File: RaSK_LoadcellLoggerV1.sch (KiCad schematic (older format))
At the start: 31 parts, among them P1 STLINK_SWD, U1 STM32F303RE, U2 TWE-Lite_DIP

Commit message: complete making schematic
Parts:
- removed C2: 0.47u, symbol C_Small
- removed VR1: NJM12888, TO_SOT_Packages_SMD:SOT-23-5, symbol NJM12888
- added C2, C4: 33u, symbol CP_Small
- added C3: 0.1u, symbol C_Small
- added J1: LoadCell, symbol Conn_01x05_Female
- added U3: Sparkfun_HX711_LoadCellAmp, KUT_Sensor:Sparkfun_HX711_LoadCellAmp_Module, symbol Sparkfun_HX711_LoadCellAmp
- added VR1, VR2: TA48Mxx, symbol TA48Mxx
- gave numbers to parts that had none: 8
- renumbered C2 to C5, C3 to C6, C4 to C7, C5 to C8, C6 to C9
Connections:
- net labels added: +5V, LCAmp_DAT, LCAmp_SCK
- wire segments 79 -> 94
- no-connect marks 39 -> 38
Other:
- moved on the sheet: P1

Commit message: connect stm32 pins to other components except for loadcell-amp (Sorry, I forgot this step...) add STLink UART debug connector add two buttons for TWE-Lite programming
p.s.
I didn't connect communication pins of loadcell-amp.
These pins can connect any stm32 digital pins.
Please connect these pins as you want.
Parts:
- removed J1: LoadCell, symbol Conn_01x05_Female
- added J1: STLINK_UART, symbol Conn_01x03_Male
- added J2: Conn_01x05_Male, symbol Conn_01x05_Male
- added SW1: TWE_RESET, symbol SW_Push
- added SW2: TWE_PRG, symbol SW_Push
- renumbered J6 to J3, J2 to J4, J4 to J5, J3 to J6, J5 to J7
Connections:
- net labels added: Debug_mIN, Debug_mOUT, TWE_mIN, TWE_mOUT
- net labels removed: TWE_MIN, TWE_MOUT, TWE_PRG, TWE_RESET
- wire segments 94 -> 103
- no-connect marks 38 -> 72

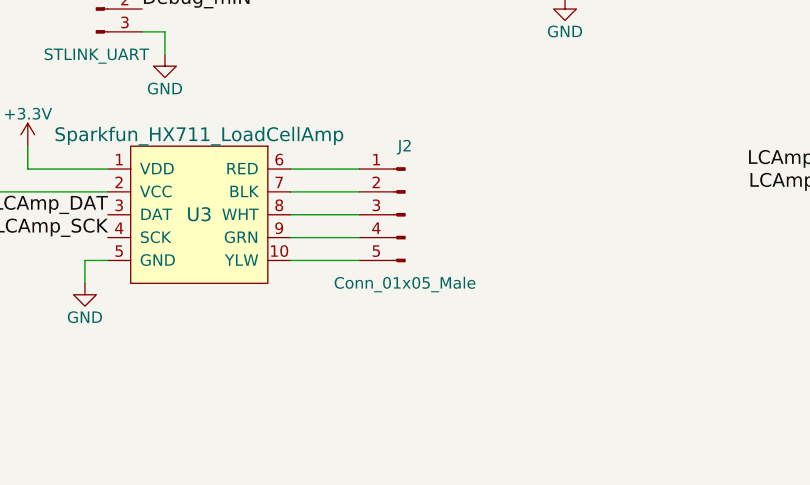
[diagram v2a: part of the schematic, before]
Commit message: fix connector J2 name
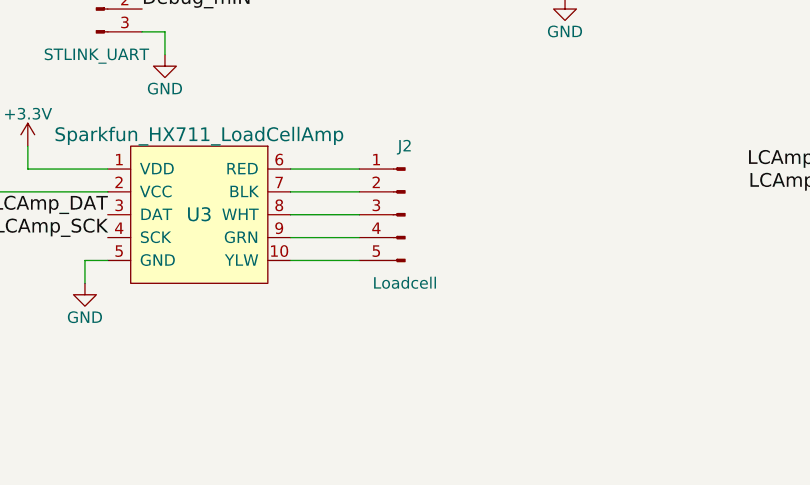
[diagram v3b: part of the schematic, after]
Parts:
- J2: value Conn_01x05_Male -> Loadcell
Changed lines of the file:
@@
 P 3050 6300
 F 0 "J2" H 3050 6600 50  0000 C CNN
-F 1 "Conn_01x05_Male" H 3050 6000 50  0000 C CNN
+F 1 "Loadcell" H 3050 6000 50  0000 C CNN
 F 2 "" H 3050 6300 50  0001 C CNN
 F 3 "" H 3050 6300 50  0001 C CNN

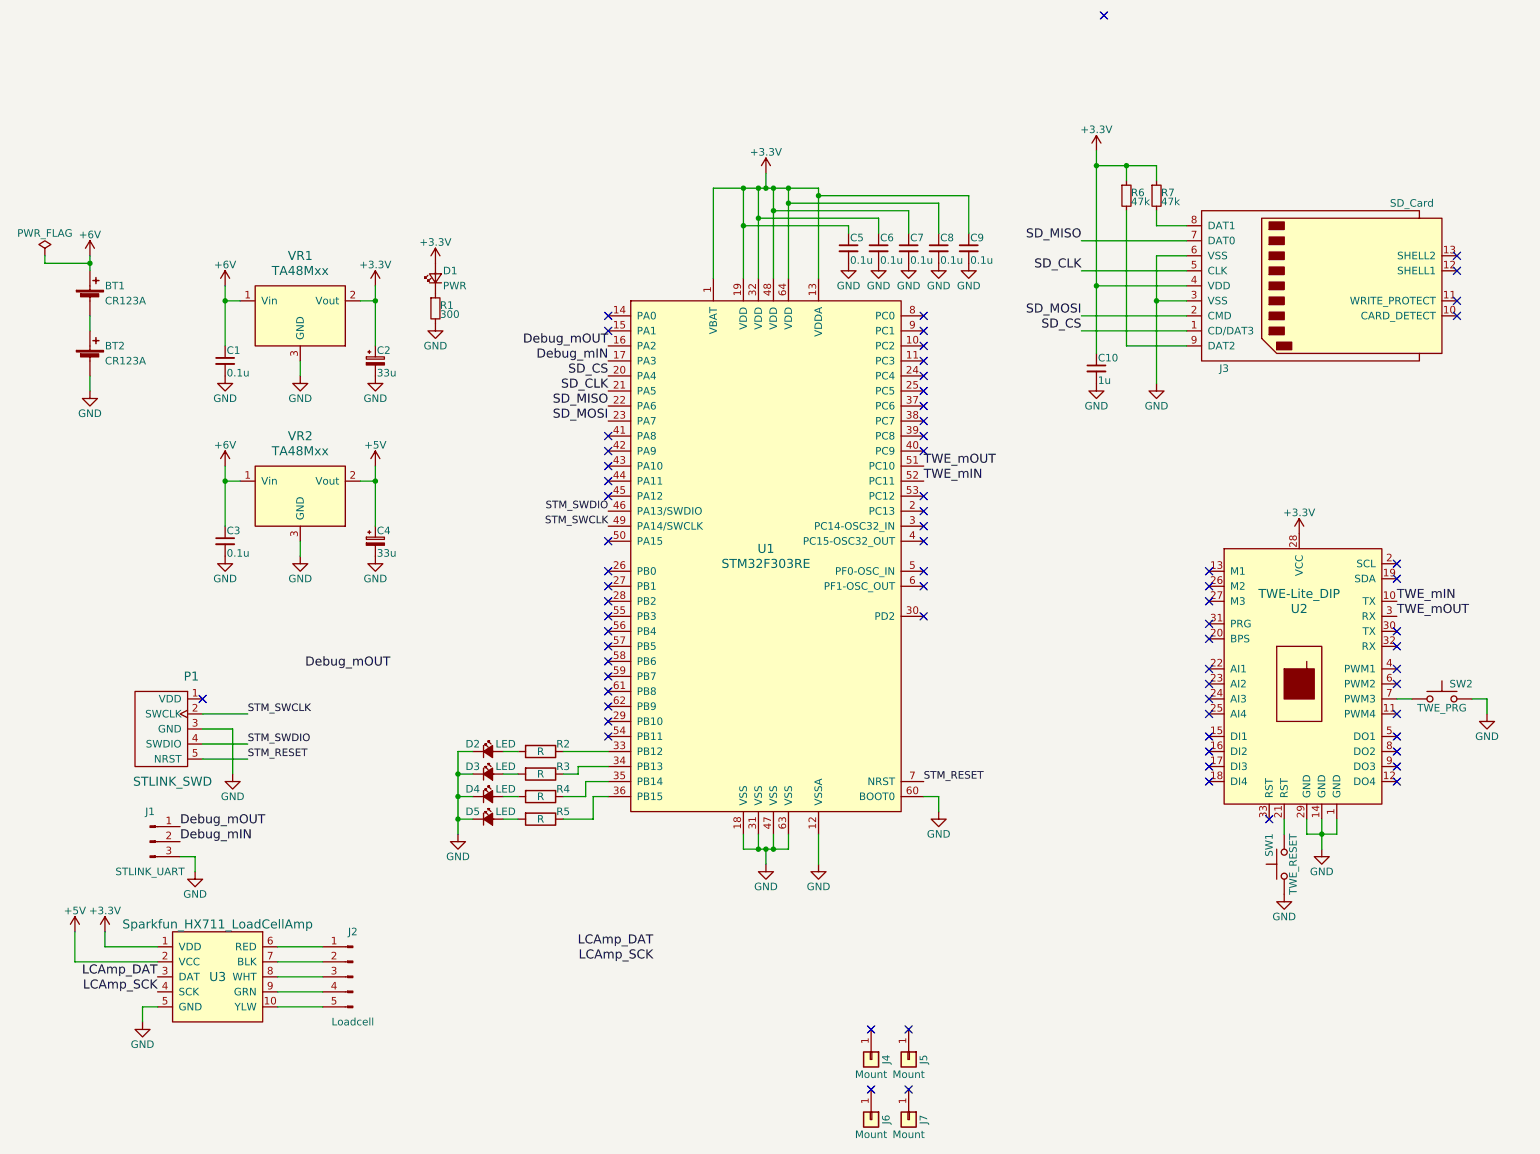
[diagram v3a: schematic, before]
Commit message: add power switch ,pass capacitor and assign footprint
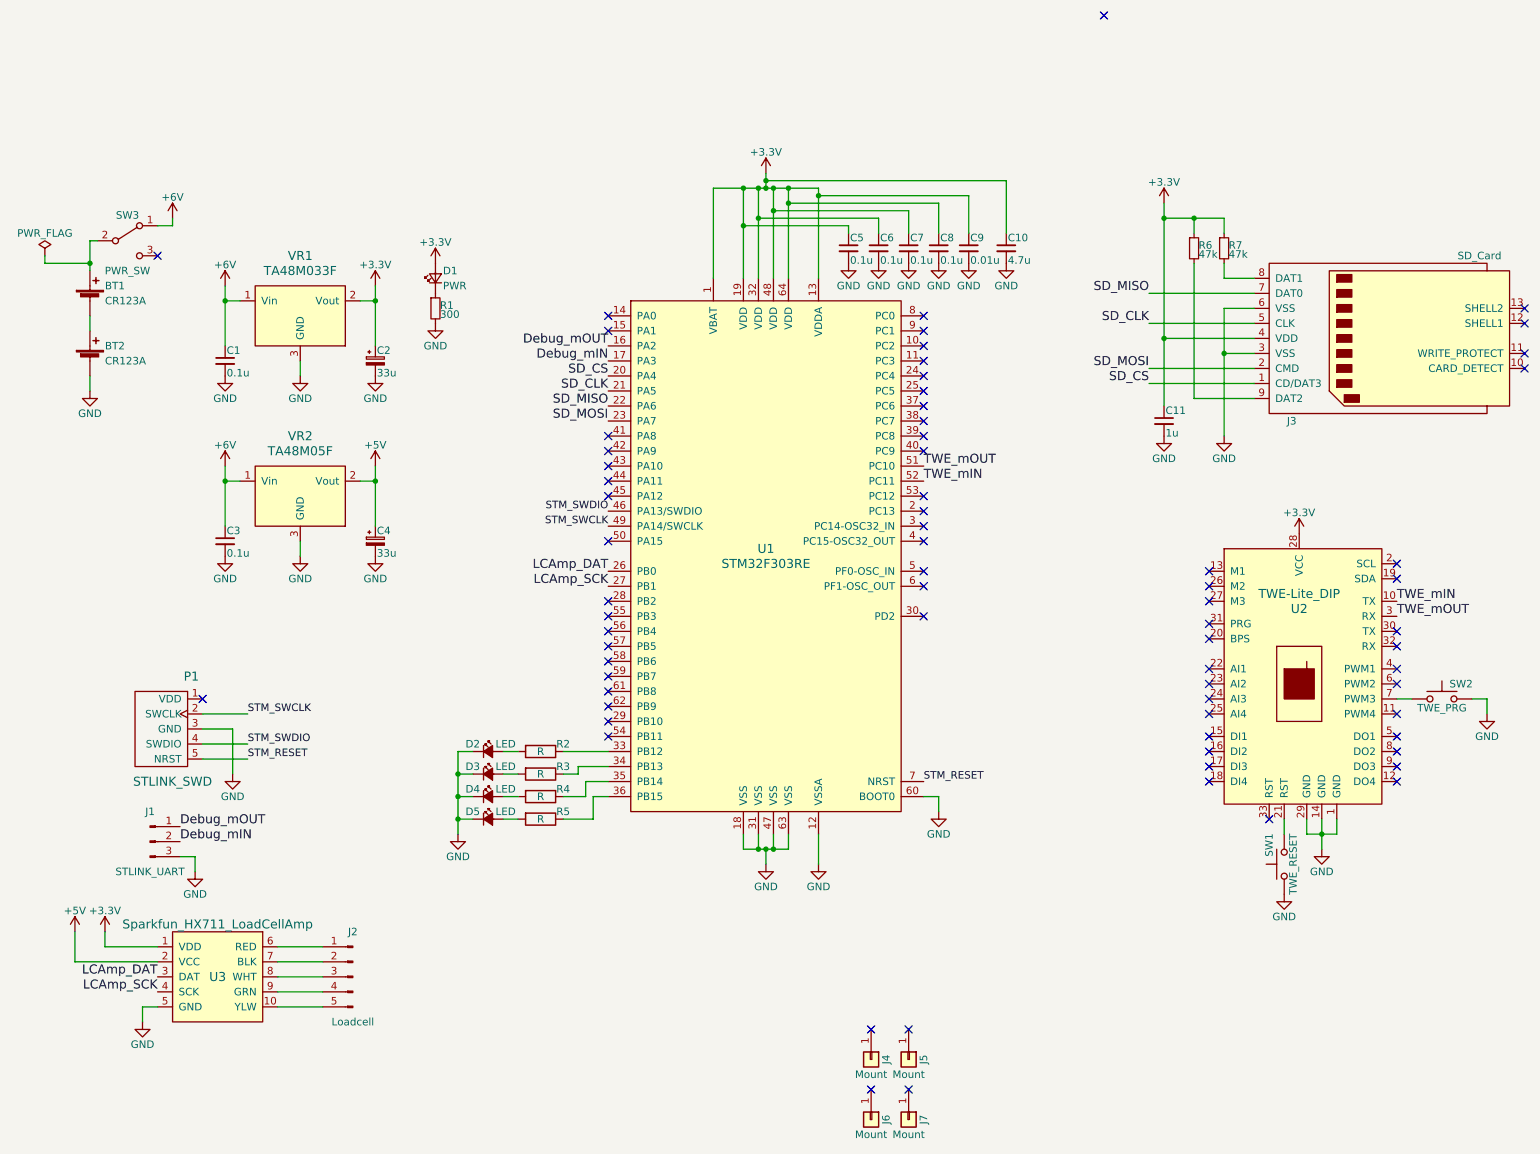
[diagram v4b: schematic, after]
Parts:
- added C10: 4.7u, Capacitors_SMD:C_1206, symbol C_Small
- added SW3: PWR_SW, KUT_Switch:ToggleSeitch_Q22, symbol SW_SPDT
- BT1, BT2: footprint (none) -> KUT_Device:BHC-CR123A
- C1, C3, C5, C6, C7, C8: footprint (none) -> Capacitors_SMD:C_0603
- C11: renamed from C10; footprint (none) -> Capacitors_SMD:C_0603
- C2, C4: footprint (none) -> Capacitors_THT:CP_Radial_D10.0mm_P2.50mm
- C9: value 0.1u -> 0.01u; footprint (none) -> Capacitors_SMD:C_0603
- D1, D2, D3, D4, D5: footprint (none) -> Diodes_SMD:D_0603
- J1: footprint (none) -> KUT_Connector:DF1E-3P_Straight
- J2, P1: footprint (none) -> KUT_Connector:DF1E-5P_Straight
- J3: footprint 10067847-001 -> KUT_Connector:AE-MICRO-SD-DIP
- J4, J5, J6, J7: footprint (none) -> Mounting_Holes:MountingHole_3.2mm_M3
- R1, R2, R3, R4, R5, R6, R7: footprint (none) -> Resistors_SMD:R_0603
- SW1, SW2: footprint (none) -> KUT_Switch:TactSwitch_1
- U2: footprint (none) -> KUT_CommIC:TWE-Lite_DIP_28P
- VR1: value TA48Mxx -> TA48M033F; footprint (none) -> KUT_Device:TA48Mxx
- VR2: value TA48Mxx -> TA48M05F; footprint (none) -> KUT_Device:TA48Mxx
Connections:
- net +3V3: now also C10.1
- net +6V: now also SW3.1 (A); no longer BT1.1 (+)
- net GND: now also C10.2
- net LCAmp_DAT: now also U1.26 (PB0)
- net LCAmp_SCK: now also U1.27 (PB1)
- new net: BT1.1 (+), SW3.2 (B)
- no-connect marks 72 -> 71
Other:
- moved on the sheet: C11, J3, R6, R7

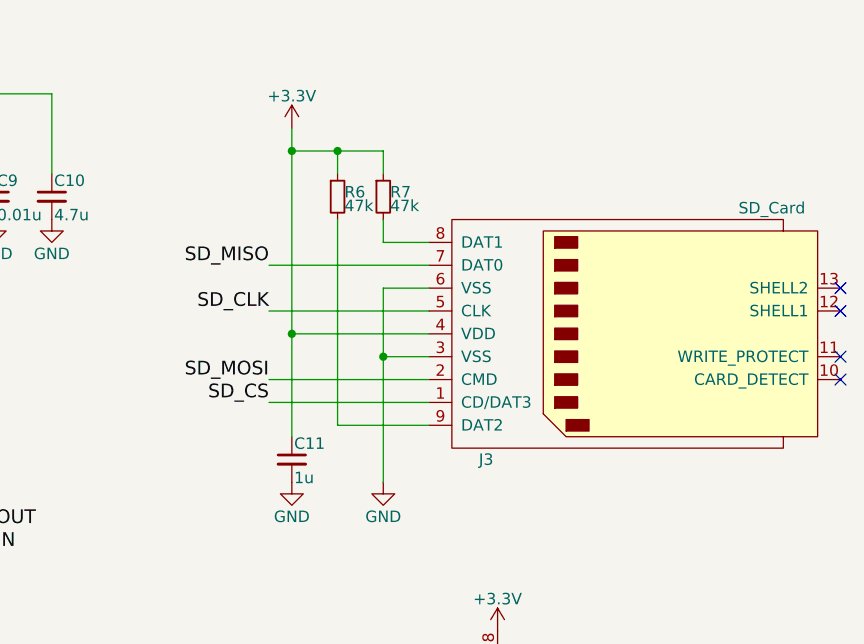
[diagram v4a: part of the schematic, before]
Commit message: change micro sd card slot to dip
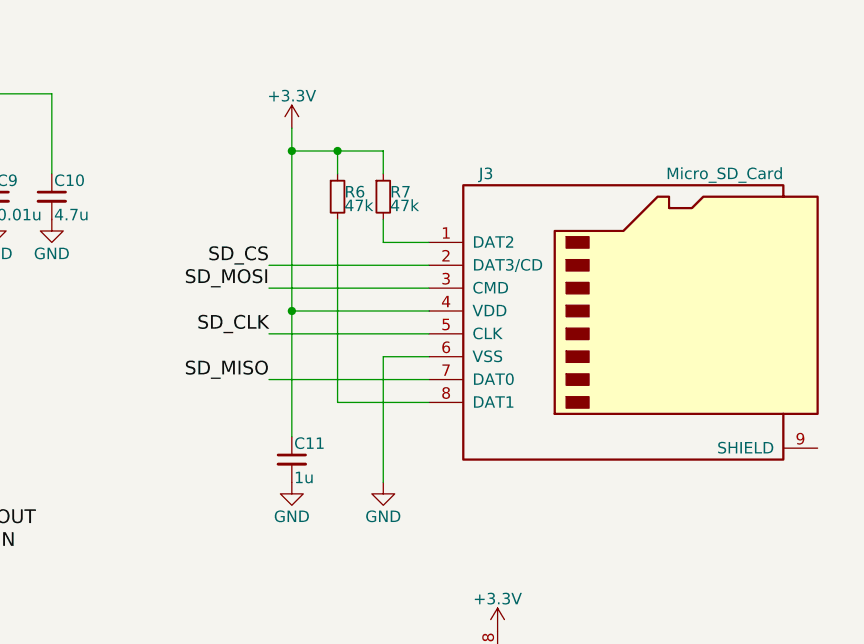
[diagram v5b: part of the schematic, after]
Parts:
- removed J3: SD_Card, KUT_Connector:AE-MICRO-SD-DIP, symbol SD_Card
- added J3: Micro_SD_Card, KUT_Connector:AE-MICRO-SD-DIP, symbol Micro_SD_Card
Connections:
- net +3V3: now also J3.4 (VDD)
- net GND: now also J3.6 (VSS)
- net SD_CLK: now also J3.5 (CLK)
- net SD_CS: now also J3.2 (DAT3/CD)
- net SD_MISO: now also J3.7 (DAT0)
- net SD_MOSI: now also J3.3 (CMD)
- net at R7.2: now also J3.1 (DAT2)
- net at R6.2: now also J3.8 (DAT1)
- no-connect marks 71 -> 67
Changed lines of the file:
@@
 TWE_mIN
-$Comp
-L SD_Card J3
-U 1 1 5A736789
-P 9950 2050
-F 0 "J3" H 9300 2600 50  0000 C CNN
-F 1 "SD_Card" H 10550 1500 50  0000 C CNN
-F 2 "KUT_Connector:AE-MICRO-SD-DIP" H 10150 2400 50  0001 C CNN
-F 3 "" H 9950 2050 50  0001 C CNN
-	1    9950 2050
-	1    0    0    1
-$EndComp
 $Comp
 L Battery_Cell BT1
@@
 	1    0    0    -1
 $EndComp
-NoConn ~ 10850 1850
-NoConn ~ 10850 1950
-NoConn ~ 10850 2150
-NoConn ~ 10850 2250
 $Comp
 L GND #PWR022
@@
 	1    0    0    -1
 $EndComp
+Text Label 8350 2250 2    60   ~ 0
+SD_MISO
+Text Label 8350 2050 2    60   ~ 0
+SD_CLK
+Text Label 8350 1850 2    60   ~ 0
+SD_MOSI
 Text Label 8350 1750 2    60   ~ 0
-SD_MISO
-Text Label 8350 1950 2    60   ~ 0
-SD_CLK
-Text Label 8350 2250 2    60   ~ 0
-SD_MOSI
-Text Label 8350 2350 2    60   ~ 0
 SD_CS
 $Comp
@@
 Connection ~ 5650 1050
 Wire Wire Line
-	8850 1850 8850 2700
-Wire Wire Line
 	8850 2150 9050 2150
 Wire Wire Line
-	9050 1850 8850 1850
-Connection ~ 8850 2150
-Wire Wire Line
 	8850 1550 8850 1650
 Wire Wire Line
 	8850 1650 9050 1650
 Wire Wire Line
-	8650 1550 8650 2450
-Wire Wire Line
-	8650 2450 9050 2450
-Wire Wire Line
 	8450 1150 8450 2500
 Wire Wire Line
-	8450 2050 9050 2050
-Wire Wire Line
 	8450 1250 8850 1250
 Wire Wire Line
 	8650 1250 8650 1350
-Connection ~ 8450 2050
 Wire Wire Line
 	8850 1250 8850 1350
@@
 Connection ~ 8450 1250
 Wire Wire Line
-	8350 1950 9050 1950
-Wire Wire Line
 	9050 1750 8350 1750
 Wire Wire Line
 	8350 2250 9050 2250
-Wire Wire Line
-	8350 2350 9050 2350
 Wire Wire Line
 	4150 4800 4050 4800
@@
 	1    0    0    -1
 $EndComp
+$Comp
+L Micro_SD_Card J3
+U 1 1 5A7DF022
+P 9950 1950
+F 0 "J3" H 9300 2550 50  0000 C CNN
+F 1 "Micro_SD_Card" H 10600 2550 50  0000 R CNN
+F 2 "KUT_Connector:AE-MICRO-SD-DIP" H 11100 2250 50  0001 C CNN
+F 3 "" H 9950 1950 50  0001 C CNN
+	1    9950 1950
+	1    0    0    -1
+$EndComp
+Wire Wire Line
+	9050 2350 8650 2350
+Wire Wire Line
+	8650 2350 8650 1550
+Wire Wire Line
+	9050 1850 8350 1850
+Wire Wire Line
+	8850 2150 8850 2700
+Wire Wire Line
+	9050 1950 8450 1950
+Connection ~ 8450 1950
+Wire Wire Line
+	9050 2050 8350 2050
 $EndSCHEMATC

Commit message: create pcb file
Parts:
- D1, D2, D3, D4, D5: footprint Diodes_SMD:D_0603 -> LEDs:LED_D3.0mm
- U1: symbol STM32F303RE -> STM32F303RE-RESCUE-RaSK_LoadcellLoggerV1
- U2: footprint KUT_CommIC:TWE-Lite_DIP_28P -> KUT_CommIC:TWE-Lite_DIP
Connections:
- net GND: now also SW1.2; no longer SW1.1
- net LCAmp_DAT: now also U1.14 (PA0); no longer U1.26 (PB0)
- net LCAmp_SCK: now also U1.15 (PA1); no longer U1.27 (PB1)
- net at U2.21 (RST): now also SW1.1; no longer SW1.2
- no-connect marks 67 -> 68
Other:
- moved on the sheet: SW1
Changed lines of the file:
@@
 EESchema Schematic File Version 2
+LIBS:RaSK_LoadcellLoggerV1-rescue
 LIBS:power
 LIBS:device
@@
 F 0 "U2" H 9350 4750 60  0000 C CNN
 F 1 "TWE-Lite_DIP" H 9350 4850 60  0000 C CNN
-F 2 "KUT_CommIC:TWE-Lite_DIP_28P" H 9300 5250 60  0001 C CNN
+F 2 "KUT_CommIC:TWE-Lite_DIP" H 9300 5250 60  0001 C CNN
 F 3 "" H 9300 5250 60  0000 C CNN
 	1    9350 4300
@@
 F 0 "D1" V 3650 1600 50  0000 R CNN
 F 1 "PWR" V 3550 1600 50  0000 R CNN
-F 2 "Diodes_SMD:D_0603" V 3600 1650 50  0001 C CNN
+F 2 "LEDs:LED_D3.0mm" V 3600 1650 50  0001 C CNN
 F 3 "" V 3600 1650 50  0001 C CNN
 	1    3600 1650
@@
 F 0 "D2" H 3800 4850 50  0000 L CNN
 F 1 "LED" H 4000 4850 50  0000 L CNN
-F 2 "Diodes_SMD:D_0603" V 3950 4800 50  0001 C CNN
+F 2 "LEDs:LED_D3.0mm" V 3950 4800 50  0001 C CNN
 F 3 "" V 3950 4800 50  0001 C CNN
 	1    3950 4800
@@
 F 0 "D3" H 3800 5000 50  0000 L CNN
 F 1 "LED" H 4000 5000 50  0000 L CNN
-F 2 "Diodes_SMD:D_0603" V 3950 4950 50  0001 C CNN
+F 2 "LEDs:LED_D3.0mm" V 3950 4950 50  0001 C CNN
 F 3 "" V 3950 4950 50  0001 C CNN
 	1    3950 4950
@@
 F 0 "D4" H 3800 5150 50  0000 L CNN
 F 1 "LED" H 4000 5150 50  0000 L CNN
-F 2 "Diodes_SMD:D_0603" V 3950 5100 50  0001 C CNN
+F 2 "LEDs:LED_D3.0mm" V 3950 5100 50  0001 C CNN
 F 3 "" V 3950 5100 50  0001 C CNN
 	1    3950 5100
@@
 F 0 "D5" H 3800 5300 50  0000 L CNN
 F 1 "LED" H 4000 5300 50  0000 L CNN
-F 2 "Diodes_SMD:D_0603" V 3950 5250 50  0001 C CNN
+F 2 "LEDs:LED_D3.0mm" V 3950 5250 50  0001 C CNN
 F 3 "" V 3950 5250 50  0001 C CNN
 	1    3950 5250
@@
 	1    0    0    -1
 $EndComp
-Text Label 4750 3600 2    60   ~ 0
+Text Label 4750 1900 2    60   ~ 0
 LCAmp_DAT
-Text Label 4750 3700 2    60   ~ 0
+Text Label 4750 2000 2    60   ~ 0
 LCAmp_SCK
 Text Label 6850 2900 0    60   ~ 0
@@
 F 3 "" H 9250 5750 50  0001 C CNN
 	1    9250 5550
-	0    -1   -1   0
+	0    1    1    0
 $EndComp
 $Comp
@@
 	1    0    0    -1
 $EndComp
-NoConn ~ 6850 1900
-NoConn ~ 6850 2000
 NoConn ~ 6850 2100
 NoConn ~ 6850 2200
@@
 NoConn ~ 6850 3100
 NoConn ~ 6850 3200
-NoConn ~ 4750 1900
-NoConn ~ 4750 2000
 NoConn ~ 4750 2700
 NoConn ~ 4750 2800
 NoConn ~ 4750 2900
-NoConn ~ 4750 3000
-NoConn ~ 4750 3100
 NoConn ~ 4750 3400
 NoConn ~ 4750 3800
-NoConn ~ 4750 3900
-NoConn ~ 4750 4000
 NoConn ~ 4750 4100
-NoConn ~ 4750 4200
-NoConn ~ 4750 4300
 NoConn ~ 4750 4400
 NoConn ~ 4750 4500
@@
 NoConn ~ 1750 1500
 $Comp
-L STM32F303RE U1
+L STM32F303RE-RESCUE-RaSK_LoadcellLoggerV1 U1
 U 1 1 5A735E94
 P 5800 3500
@@
 Wire Wire Line
 	9050 2050 8350 2050
+NoConn ~ 4750 3600
+NoConn ~ 4750 3700
+NoConn ~ 4750 3000
+NoConn ~ 4750 3100
+NoConn ~ 4750 4000
+NoConn ~ 4750 3900
+NoConn ~ 10750 2550
+NoConn ~ 6850 1900
+NoConn ~ 6850 2000
+NoConn ~ 4750 4200
+NoConn ~ 4750 4300
 $EndSCHEMATC
